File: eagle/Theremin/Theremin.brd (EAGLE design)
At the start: 161 x 101.6 mm, 57 parts, among them Q8 2N3904, U1 LM78L12, U2 LM79L12

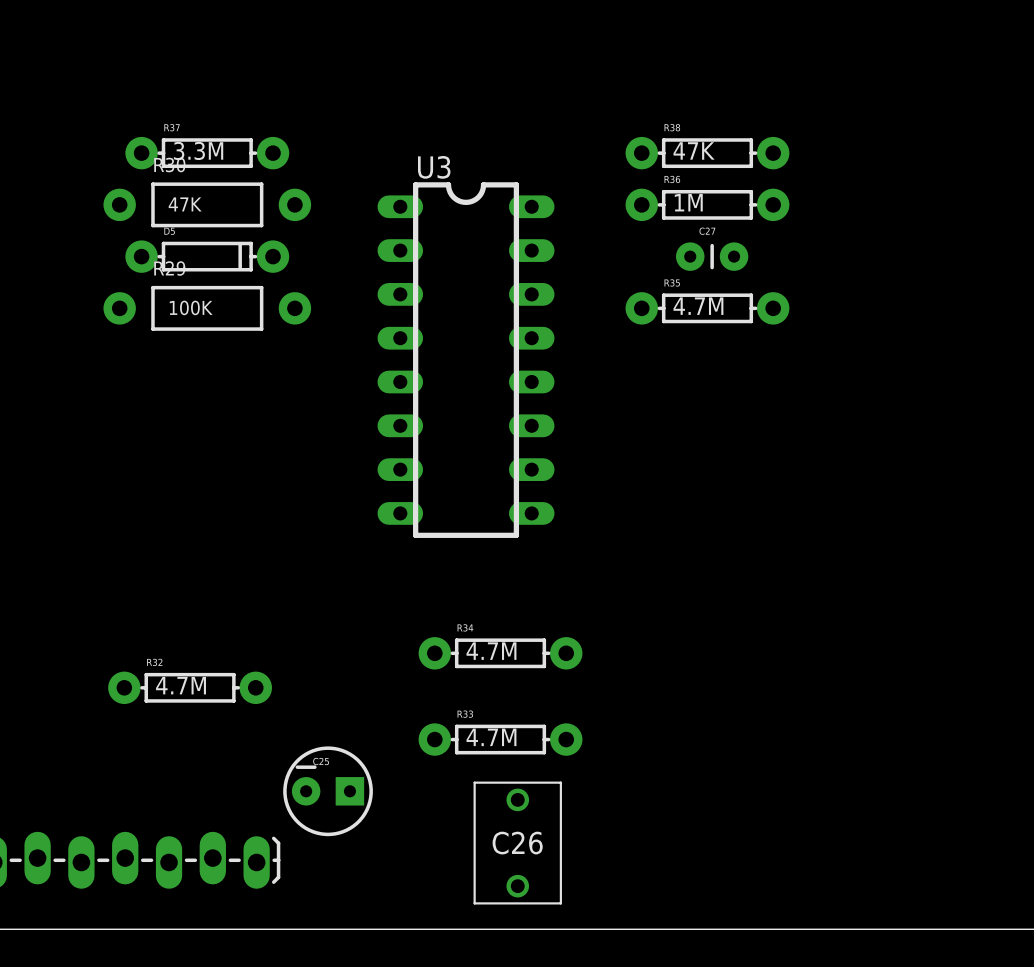
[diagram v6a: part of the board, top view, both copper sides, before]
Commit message: Finish VOLTAGE CONTROLLED AMP, add DETECTOR
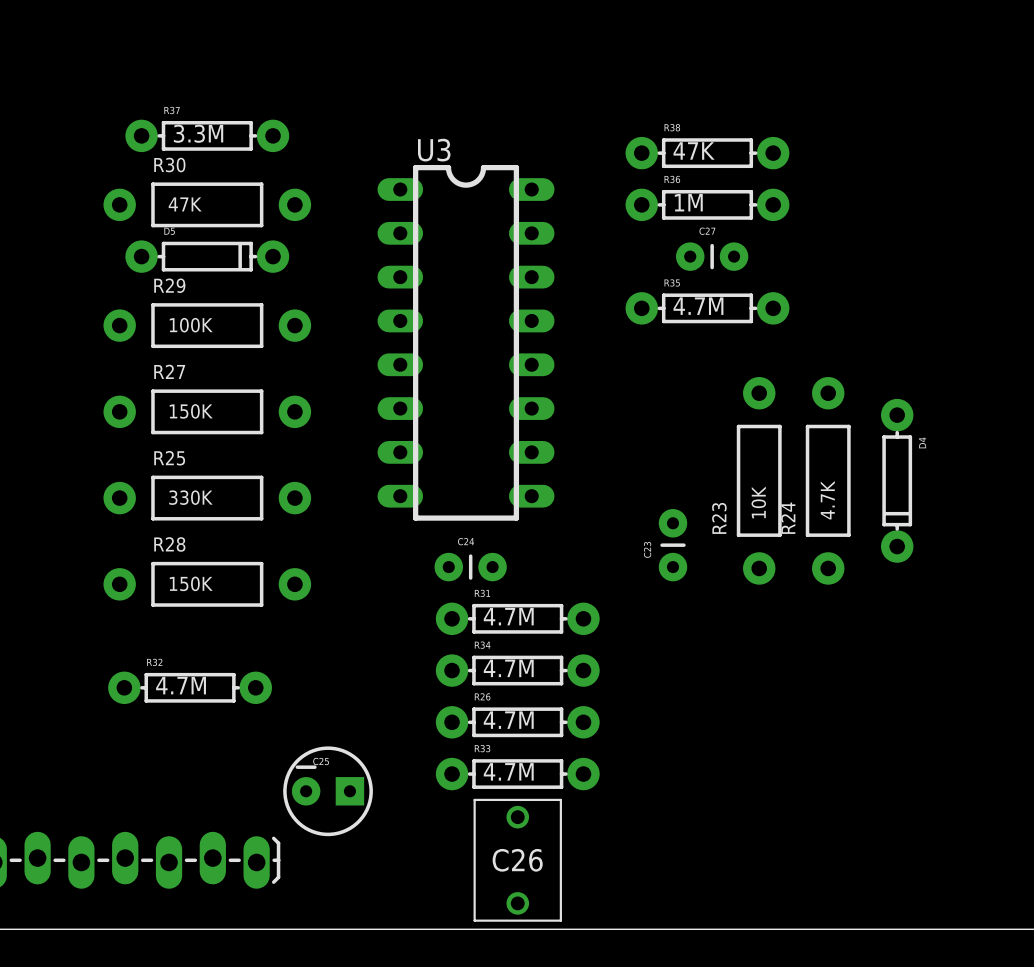
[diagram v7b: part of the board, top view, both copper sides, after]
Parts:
- added C23: 4700pF, SparkFun-Capacitors:CAP-PTH-SMALL
- added C24: 3300pF, SparkFun-Capacitors:CAP-PTH-SMALL
- added D4: (no value), SparkFun-DiscreteSemi:DIODE-1N4148
- added R23: 10K, SparkFun-Resistors:AXIAL-0.4
- added R24: 4.7K, SparkFun-Resistors:AXIAL-0.4
- added R25: 330K, SparkFun-Resistors:AXIAL-0.4
- added R26, R31: 4.7M, SparkFun-Passives:AXIAL-0.3EZ
- added R27, R28: 150K, SparkFun-Resistors:AXIAL-0.4
- moved R33 2.24 mm to (88.0, 9.00)
- moved R34 1.41 mm to (88.0, 15.0)
- moved C26 1.00 mm to (88.0, 4.00)
- moved R29 1.00 mm to (70.0, 35.0)
- moved R37 1.00 mm to (70.0, 46.0)
- moved U3 1.00 mm to (85.0, 34.0)
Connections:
- new net N$32: C24.2, R31.P$2, U3.5, U3.7
- new net N$33: R27.P$2, U3.2
- new net N$34: JP2.9, R27.P$1
- new net N$35: JP2.7, R28.P$1
- new net N$36: R25.P$2, R26.P$2, R28.P$2, U3.4
- new net N$37: C23.1, JP1.7, R23.P$2, R24.P$1
- new net N$38: C23.2, D4.C, R24.P$2
- new net VNEG: R25.P$1
- net GND: now also C24.1, R26.P$1, R31.P$1
- net N$20: now also D4.A, R23.P$1

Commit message: work on POWER SUPPLY
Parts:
- added C21, C22: 0.1uF, SparkFun-Capacitors:CAP-PTH-SMALL
- added JP3: POWER IN, SparkFun-Connectors:1X02_LOCK
- moved JP2 6.00 mm to (44.0, 4.00)
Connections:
- new net N$39: JP2.1, JP3.2
- net -12V: no longer JP2.3
- net 5V: now also C21.1, U1.3
- net GND: now also C21.2, C22.1, JP3.1
- net N$14: now also JP2.2
- net VNEG: now also C22.2, JP2.3, U2.1
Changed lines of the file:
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@@
 <element name="R36" library="SparkFun-Passives" package="AXIAL-0.3EZ" value="1M" x="99" y="42"/>
 <element name="R35" library="SparkFun-Passives" package="AXIAL-0.3EZ" value="4.7M" x="99" y="36"/>
-<element name="JP2" library="SparkFun-Connectors" package="1X10_LOCK_LONGPADS" value="Front Panel" x="50" y="4"/>
+<element name="JP2" library="SparkFun-Connectors" package="1X10_LOCK_LONGPADS" value="Front Panel" x="44" y="4"/>
 <element name="R30" library="SparkFun-Resistors" package="AXIAL-0.4" value="47K" x="70" y="42"/>
 <element name="R29" library="SparkFun-Resistors" package="AXIAL-0.4" value="100K" x="70" y="35"/>
@@
 <element name="D4" library="SparkFun-DiscreteSemi" package="DIODE-1N4148" value="" x="110" y="26" rot="R270"/>
 <element name="R24" library="SparkFun-Resistors" package="AXIAL-0.4" value="4.7K" x="106" y="26" rot="R90"/>
+<element name="C21" library="SparkFun-Capacitors" package="CAP-PTH-SMALL" value="0.1uF" x="68" y="75" rot="R270"/>
+<element name="C22" library="SparkFun-Capacitors" package="CAP-PTH-SMALL" value="0.1uF" x="68" y="80" rot="R90"/>
+<element name="JP3" library="SparkFun-Connectors" package="1X02_LOCK" value="POWER IN" x="20" y="88"/>
 </elements>
 <signals>
@@
 <contactref element="U3" pad="14"/>
 <contactref element="C27" pad="1"/>
-<contactref element="JP2" pad="4"/>
 <contactref element="C26" pad="P$1"/>
 <contactref element="R34" pad="P$2"/>
@@
 <contactref element="C24" pad="1"/>
 <contactref element="R26" pad="P$1"/>
+<contactref element="C21" pad="2"/>
+<contactref element="C22" pad="1"/>
+<contactref element="JP2" pad="4"/>
+<contactref element="JP3" pad="1"/>
 <wire x1="118.54" y1="68" x2="131" y2="80" width="0" layer="19" extent="1-1"/>
 <wire x1="92.9725" y1="70.025" x2="118.54" y2="68" width="0" layer="19" extent="1-1"/>
@@
 <wire x1="88.81" y1="37.81" x2="82.2325" y2="58.46" width="0" layer="19" extent="1-1"/>
 <wire x1="98" y1="39" x2="88.81" y2="37.81" width="0" layer="19" extent="1-1"/>
-<wire x1="91.81" y1="15" x2="88.81" y2="37.81" width="0" layer="19" extent="1-1"/>
-<wire x1="88" y1="6.5" x2="91.81" y2="15" width="0" layer="19" extent="1-1"/>
+<wire x1="84" y1="21" x2="88.81" y2="37.81" width="0" layer="19" extent="1-1"/>
+<wire x1="84.19" y1="18" x2="84" y2="21" width="0" layer="19" extent="1-1"/>
+<wire x1="84.19" y1="12" x2="84.19" y2="18" width="0" layer="19" extent="1-1"/>
+<wire x1="88" y1="6.5" x2="84.19" y2="12" width="0" layer="19" extent="1-1"/>
+<wire x1="91.81" y1="15" x2="84.19" y2="18" width="0" layer="19" extent="1-1"/>
+<wire x1="51.62" y1="3.873" x2="84.19" y2="12" width="0" layer="19" extent="1-1"/>
 <wire x1="141.73" y1="52" x2="118.54" y2="68" width="0" layer="19" extent="1-1"/>
 <wire x1="147.25" y1="43" x2="141.73" y2="52" width="0" layer="19" extent="1-1"/>
 <wire x1="156.75" y1="43" x2="147.25" y2="43" width="0" layer="19" extent="1-1"/>
-<wire x1="57.62" y1="3.873" x2="88" y2="6.5" width="0" layer="19" extent="1-1"/>
 <wire x1="132" y1="10.92" x2="147.25" y2="43" width="0" layer="19" extent="1-1"/>
 <wire x1="157.08" y1="4" x2="132" y2="10.92" width="0" layer="19" extent="1-1"/>
-<wire x1="23.48" y1="17.13" x2="57.62" y2="3.873" width="0" layer="19" extent="1-1"/>
+<wire x1="23.48" y1="17.13" x2="51.62" y2="3.873" width="0" layer="19" extent="1-1"/>
 <wire x1="10.78" y1="12.05" x2="23.48" y2="17.13" width="0" layer="19" extent="1-1"/>
 <wire x1="29" y1="31" x2="23.48" y2="17.13" width="0" layer="19" extent="1-1"/>
-<wire x1="84" y1="21" x2="10.78" y2="12.05" width="0" layer="19" extent="1-1"/>
-<wire x1="84.19" y1="18" x2="84" y2="21" width="0" layer="19" extent="1-1"/>
-<wire x1="84.19" y1="12" x2="84.19" y2="18" width="0" layer="19" extent="1-1"/>
+<wire x1="68" y1="72.46" x2="10.78" y2="12.05" width="0" layer="19" extent="1-1"/>
+<wire x1="68" y1="80" x2="68" y2="72.46" width="0" layer="19" extent="1-1"/>
+<wire x1="19.8222" y1="88" x2="68" y2="80" width="0" layer="19" extent="1-1"/>
 <wire x1="4.43" y1="29.83" x2="10.78" y2="12.05" width="0" layer="19" extent="1-1"/>
 <wire x1="4.43" y1="33.64" x2="4.43" y2="29.83" width="0" layer="19" extent="1-1"/>
@@
 <contactref element="R18" pad="P$1"/>
 <contactref element="JP2" pad="6"/>
-<wire x1="62.7" y1="3.873" x2="4.43" y2="18.4" width="0" layer="19" extent="1-1"/>
+<wire x1="56.7" y1="3.873" x2="4.43" y2="18.4" width="0" layer="19" extent="1-1"/>
 </signal>
 <signal name="-12V">
@@
 <contactref element="U3" pad="6"/>
 <contactref element="JP1" pad="5"/>
-<contactref element="JP2" pad="3"/>
 <contactref element="R32" pad="P$1"/>
 <contactref element="R29" pad="P$1"/>
 <wire x1="141" y1="14.92" x2="141.16" y2="80" width="0" layer="19" extent="1-1"/>
 <wire x1="81.19" y1="30.19" x2="141" y2="14.92" width="0" layer="19" extent="1-1"/>
-<wire x1="55.08" y1="4.127" x2="81.19" y2="30.19" width="0" layer="19" extent="1-1"/>
-<wire x1="23.48" y1="9.51" x2="55.08" y2="4.127" width="0" layer="19" extent="1-1"/>
-<wire x1="23.48" y1="12.05" x2="23.48" y2="9.51" width="0" layer="19" extent="1-1"/>
-<wire x1="23.48" y1="14.59" x2="23.48" y2="12.05" width="0" layer="19" extent="1-1"/>
-<wire x1="64.92" y1="35" x2="23.48" y2="9.51" width="0" layer="19" extent="1-1"/>
+<wire x1="64.92" y1="35" x2="81.19" y2="30.19" width="0" layer="19" extent="1-1"/>
 <wire x1="65.19" y1="14" x2="64.92" y2="35" width="0" layer="19" extent="1-1"/>
+<wire x1="23.48" y1="14.59" x2="65.19" y2="14" width="0" layer="19" extent="1-1"/>
+<wire x1="23.48" y1="12.05" x2="23.48" y2="14.59" width="0" layer="19" extent="1-1"/>
+<wire x1="23.48" y1="9.51" x2="23.48" y2="12.05" width="0" layer="19" extent="1-1"/>
 </signal>
 <signal name="N$6">
@@
 <contactref element="D3" pad="C"/>
 <contactref element="D2" pad="A"/>
+<contactref element="JP2" pad="2"/>
 <wire x1="62.23" y1="79.0575" x2="79.375" y2="80.3275" width="0" layer="19" extent="1-1"/>
+<wire x1="46.54" y1="3.873" x2="62.23" y2="79.0575" width="0" layer="19" extent="1-1"/>
 </signal>
 <signal name="N$15">
@@
 <contactref element="R35" pad="P$2"/>
 <contactref element="JP2" pad="8"/>
+<contactref element="U1" pad="3"/>
+<contactref element="C21" pad="1"/>
 <wire x1="144.27" y1="52" x2="143.7" y2="80" width="0" layer="19" extent="1-1"/>
 <wire x1="148.5" y1="46.5" x2="144.27" y2="52" width="0" layer="19" extent="1-1"/>
@@
 <wire x1="102.81" y1="36" x2="102.81" y2="42" width="0" layer="19" extent="1-1"/>
 <wire x1="88.81" y1="30.19" x2="102.81" y2="36" width="0" layer="19" extent="1-1"/>
-<wire x1="67.78" y1="3.873" x2="88.81" y2="30.19" width="0" layer="19" extent="1-1"/>
-<wire x1="29.83" y1="41.26" x2="67.78" y2="3.873" width="0" layer="19" extent="1-1"/>
-<wire x1="27.6" y1="56.19" x2="29.83" y2="41.26" width="0" layer="19" extent="1-1"/>
+<wire x1="74.6125" y1="62.865" x2="102.81" y2="45" width="0" layer="19" extent="1-1"/>
+<wire x1="61.78" y1="3.873" x2="88.81" y2="30.19" width="0" layer="19" extent="1-1"/>
+<wire x1="27.6" y1="56.19" x2="74.6125" y2="62.865" width="0" layer="19" extent="1-1"/>
 <wire x1="18.4" y1="51.42" x2="27.6" y2="56.19" width="0" layer="19" extent="1-1"/>
+<wire x1="29.83" y1="41.26" x2="27.6" y2="56.19" width="0" layer="19" extent="1-1"/>
+<wire x1="68" y1="75" x2="29.83" y2="41.26" width="0" layer="19" extent="1-1"/>
 </signal>
 <signal name="N$17">
@@
 <contactref element="C26" pad="P$2"/>
 <contactref element="R34" pad="P$1"/>
-<wire x1="91.81" y1="9" x2="72.86" y2="3.873" width="0" layer="19" extent="1-1"/>
+<wire x1="91.81" y1="9" x2="66.86" y2="3.873" width="0" layer="19" extent="1-1"/>
 <wire x1="88" y1="1.5" x2="91.81" y2="9" width="0" layer="19" extent="1-1"/>
 <wire x1="84.19" y1="15" x2="88" y2="1.5" width="0" layer="19" extent="1-1"/>
@@
 <contactref element="JP2" pad="9"/>
 <contactref element="R27" pad="P$1"/>
-<wire x1="64.92" y1="30" x2="70.32" y2="4.127" width="0" layer="19" extent="1-1"/>
+<wire x1="64.92" y1="30" x2="64.32" y2="4.127" width="0" layer="19" extent="1-1"/>
 </signal>
 <signal name="N$33">
@@
 <contactref element="JP2" pad="7"/>
 <contactref element="R28" pad="P$1"/>
-<wire x1="64.92" y1="20" x2="65.24" y2="4.127" width="0" layer="19" extent="1-1"/>
+<wire x1="64.92" y1="20" x2="59.24" y2="4.127" width="0" layer="19" extent="1-1"/>
 </signal>
 <signal name="N$36">
@@
 <signal name="VNEG">
 <contactref element="R25" pad="P$1"/>
+<contactref element="U2" pad="1"/>
+<contactref element="C22" pad="2"/>
+<contactref element="JP2" pad="3"/>
+<wire x1="64.92" y1="25" x2="73.9775" y2="78.4225" width="0" layer="19" extent="1-1"/>
+<wire x1="49.08" y1="4.127" x2="64.92" y2="25" width="0" layer="19" extent="1-1"/>
+<wire x1="68" y1="82.54" x2="49.08" y2="4.127" width="0" layer="19" extent="1-1"/>
 </signal>
 <signal name="N$37">
@@
 <wire x1="97" y1="23.54" x2="110" y2="22.19" width="0" layer="19" extent="1-1"/>
 </signal>
+<signal name="N$39">
+<contactref element="JP3" pad="2"/>
+<contactref element="JP2" pad="1"/>
+<wire x1="22.7178" y1="88" x2="44" y2="4.127" width="0" layer="19" extent="1-1"/>
+</signal>
 </signals>
